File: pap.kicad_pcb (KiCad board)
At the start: 2 copper layers, 36 x 19 mm, 6 parts, among them J1 Conn_01x03

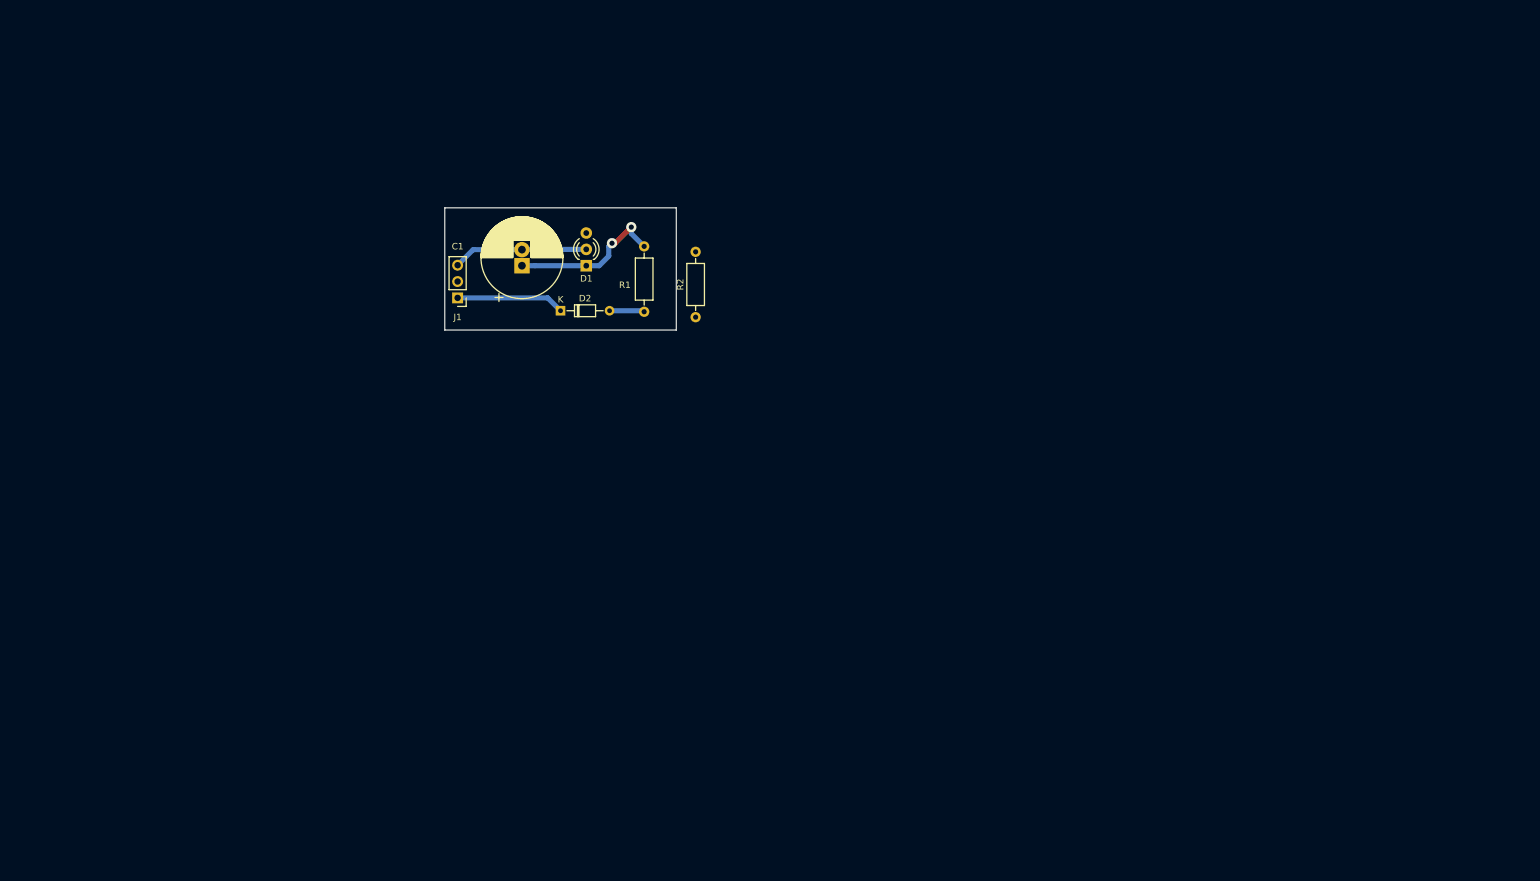
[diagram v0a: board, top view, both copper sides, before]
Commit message: agrego mas conectores y paso a pcb (todo mal!)
agregue conectores RJ45 para el encadenamiento spi y busyflag, pero no
para pulse.. es lo voy a mandar aparte porque es individual por cada
driver.. al igual que switch, y vere si alguna cosa mas.. en el rj me
sobran aun 2 pines.. ya vere que mando..lastima que no puedo mandar
pulse por ahi.. porque al ser 1 por driver necesito ir directo desde el
controlador.. sino como?... pase a pcb para ver que onda nada mas y
obvio me faltan definir los footprints de casi todo.. pero al menos
paso...orcad ya estaria llorando y no podria hacer nada...como sea, esta
bueno...sigo
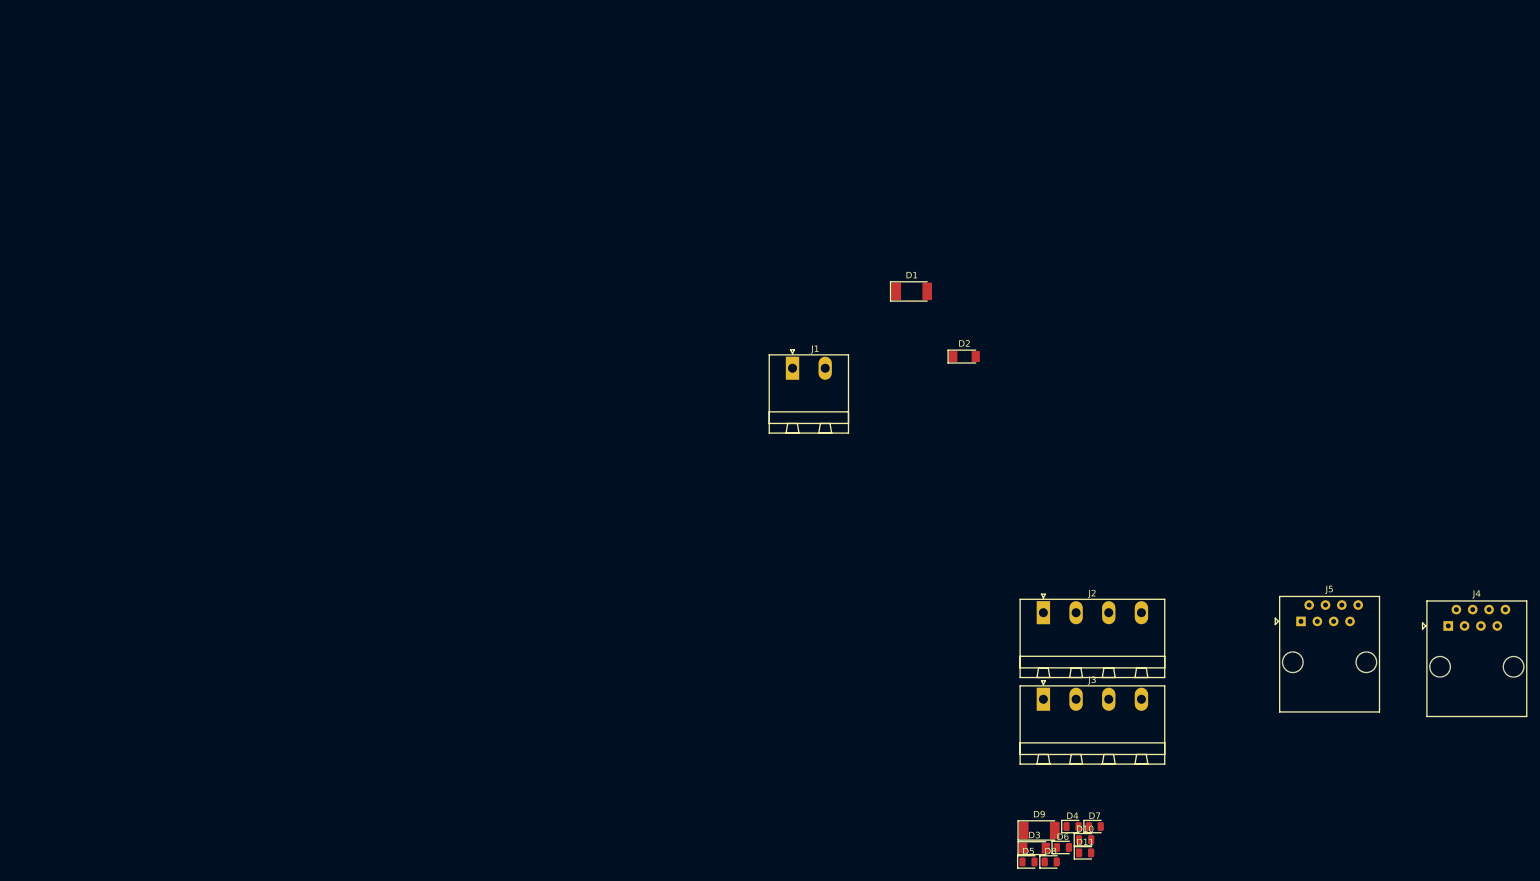
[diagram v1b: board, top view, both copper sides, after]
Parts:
- removed C1: 100n, Capacitor_THT:CP_Radial_D12.5mm_P2.50mm
- removed R1, R2: 100k, Resistor_THT:R_Axial_DIN0207_L6.3mm_D2.5mm_P10.16mm_Horizontal
- added D10: LED, LED_SMD:LED_0805_2012Metric, F.Cu at (221.5, 170.2)
- added D11: LED, LED_SMD:LED_0805_2012Metric, F.Cu at (221.5, 172.3)
- added D3: LL4148, Diode_SMD:D_MiniMELF, F.Cu at (213.7, 171.5)
- added D4: LED, LED_SMD:LED_0805_2012Metric, F.Cu at (219.6, 168.2)
- added D5: LED, LED_SMD:LED_0805_2012Metric, F.Cu at (212.7, 173.7)
- added D6: LED, LED_SMD:LED_0805_2012Metric, F.Cu at (218.1, 171.4)
- added D7: LED, LED_SMD:LED_0805_2012Metric, F.Cu at (223.0, 168.2)
- added D8: LED, LED_SMD:LED_0805_2012Metric, F.Cu at (216.2, 173.7)
- added D9: SM4007, Diode_SMD:D_MELF, F.Cu at (214.4, 168.8)
- added J2: Conn_01x04, Connector_Phoenix_MSTB:PhoenixContact_MSTBA_2,5_4-G-5,08_1x04_P5.08mm_Horizontal, F.Cu at (215.1, 134.9)
- added J3: Conn_01x04, Connector_Phoenix_MSTB:PhoenixContact_MSTBA_2,5_4-G-5,08_1x04_P5.08mm_Horizontal, F.Cu at (215.1, 148.4)
- added J4: RJ45, Connector_RJ:RJ45_Amphenol_54602-x08_Horizontal, F.Cu at (278.0, 137.0)
- added J5: RJ45, Connector_RJ:RJ45_Amphenol_54602-x08_Horizontal, F.Cu at (255.1, 136.3)
- D1: value led rojo 3mm -> SM4007; footprint LED_THT:LED_D3.0mm-3 -> Diode_SMD:D_MELF
- D2: value 1N4148 -> LL4148; footprint Diode_THT:D_DO-34_SOD68_P7.62mm_Horizontal -> Diode_SMD:D_MiniMELF
- J1: value Conn_01x03 -> Conn_01x02; footprint Connector_PinHeader_2.54mm:PinHeader_1x03_P2.54mm_Vertical -> Connector_Phoenix_MSTB:PhoenixContact_MSTBA_2,5_2-G-5,08_1x02_P5.08mm_Horizontal
- moved D2 63.2 mm to (202.8, 95.1)
- moved J1 53.2 mm to (176.1, 96.9), turned to 0 degrees
- moved D1 50.8 mm to (194.6, 85.0), turned to 0 degrees
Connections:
- D1 pad 1: Net-(C1-Pad1) -> +VDC
- D1 pad 2: Net-(C1-Pad2) -> GND
- D2 pad 1: Net-(D2-Pad1) -> Net-(C4-Pad1)
- J1 pad 1: Net-(D2-Pad1) -> GND
- J1 pad 2: Net-(J1-Pad2) -> +VDC
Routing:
- net Net-(C1-Pad1): track 24.2 -> 0.00 mm, vias 2 -> 0
- net Net-(C1-Pad2): track 21.0 -> 0.00 mm
- net Net-(D2-Pad1): track 16.8 -> 0.00 mm
- net Net-(C5-Pad2): track 5.45 -> 0.00 mm
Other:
- board outline removed

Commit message: armo huella step01 y asigno casi todas las huellas
ahi hice el landpattern del steo01, que es un parto, pero quedo bueno..
al tiempo que aprendi a editar y la verdad es que es comodo.. me animo a
decir que supera a allegro, y de hecho se parece demasiado en muchas
cosas.. huele a copia de algun lado.. incluiso los nombres en los menus
son iguales... como sea, ya quedo eso, lo que si tuve que volar algunos
pines repetidos en el simbolo porque sino era un chino tener muchos
pines repetidos, o sea en la huella tengo un pin que va a parar a
multiples pines en el esquemativo. si bien lo logre hacer superponiendo
encimados los pines en el esquemativo y dejandolos invisibles excepto
uno, eso funca, pero es un azco... preferi volar todos y dejar la union
univoca y listo.. al simbolo le faltan pines, pero el landpattern no los
necesita porque se unen todos en una misma masa de pad. despues pase
todas las huellas del resto del chiquitaje y ademas acomodo los power
netlist que estaban mal y de paso voy puliendo el disenio en general..
va quedando.. un poco mas y paso a tirar pista
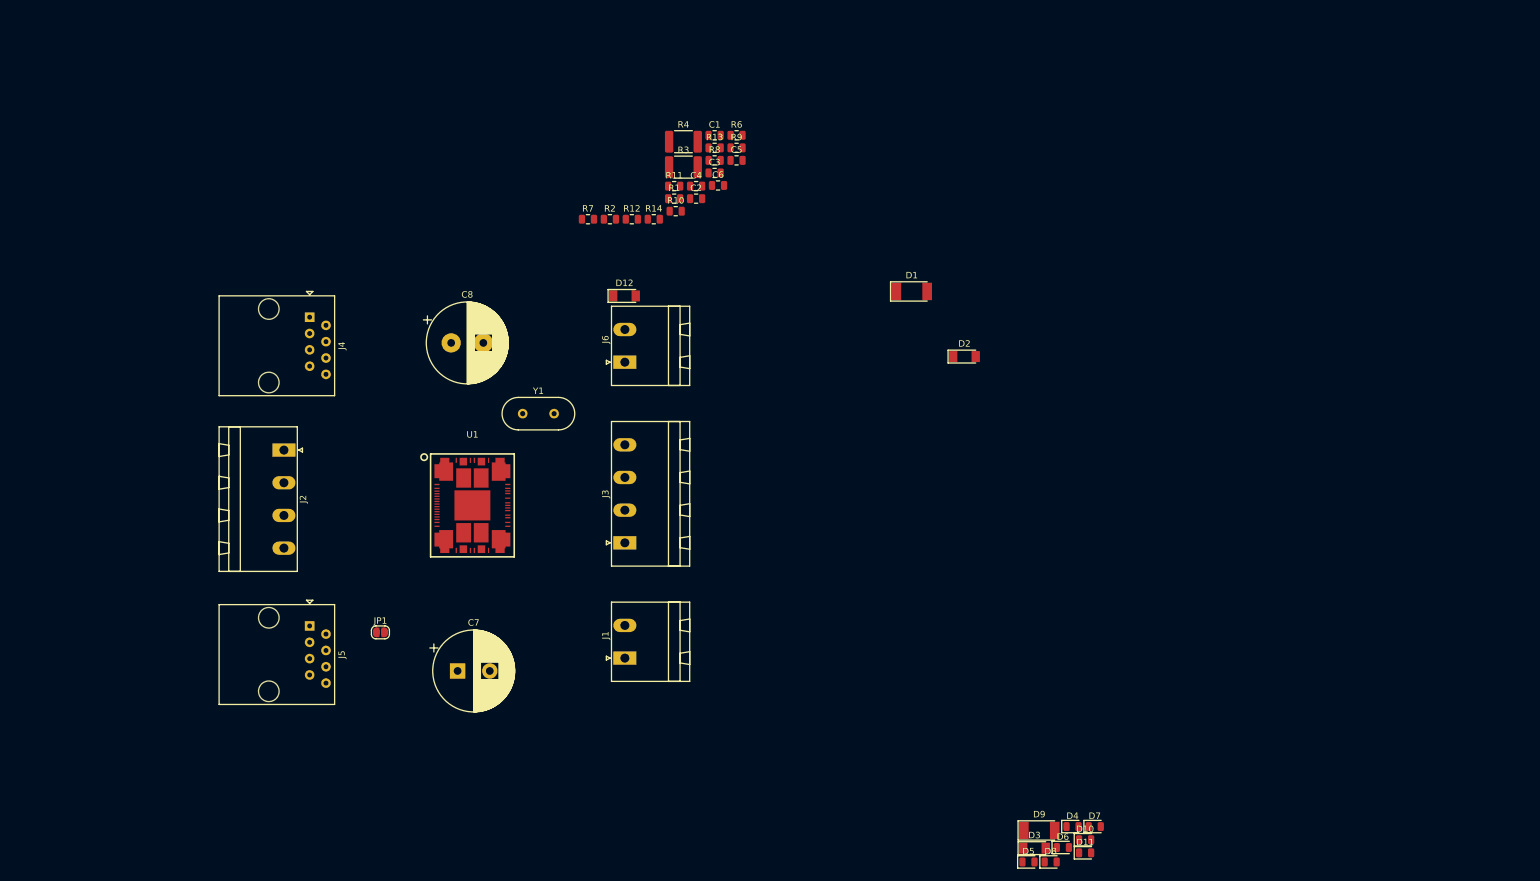
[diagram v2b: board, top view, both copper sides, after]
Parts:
- added C1: C, Capacitor_SMD:C_0805_2012Metric, F.Cu at (164.0, 60.7)
- added C2: 10pF, Capacitor_SMD:C_0805_2012Metric, F.Cu at (161.1, 70.6)
- added C3: 10pF, Capacitor_SMD:C_0805_2012Metric, F.Cu at (164.0, 66.6)
- added C4: C, Capacitor_SMD:C_0805_2012Metric, F.Cu at (161.1, 68.6)
- added C5: C, Capacitor_SMD:C_0805_2012Metric, F.Cu at (167.4, 64.6)
- added C6: C, Capacitor_SMD:C_0805_2012Metric, F.Cu at (164.5, 68.5)
- added C7: 100uFx100v, Capacitor_THT:CP_Radial_D12.5mm_P5.00mm, F.Cu at (124.0, 144.0)
- added C8: 100uFx100v, Capacitor_THT:CP_Radial_D12.5mm_P5.00mm, F.Cu at (123.0, 93.0)
- added D12: D_Zener, Diode_SMD:D_MiniMELF, F.Cu at (149.9, 85.7)
- added J6: Conn_01x02, Connector_Phoenix_MSTB:PhoenixContact_MSTBA_2,5_2-G-5,08_1x02_P5.08mm_Horizontal, F.Cu at (150.0, 96.0)
- added JP1: jumper, Jumper:SolderJumper-2_P1.3mm_Open_RoundedPad1.0x1.5mm, F.Cu at (112.0, 138.0)
- added R1: R, Resistor_SMD:R_0805_2012Metric, F.Cu at (157.7, 70.6)
- added R10: R, Resistor_SMD:R_0805_2012Metric, F.Cu at (157.9, 72.5)
- added R11: R, Resistor_SMD:R_0805_2012Metric, F.Cu at (157.7, 68.6)
- added R12: R, Resistor_SMD:R_0805_2012Metric, F.Cu at (151.1, 73.8)
- added R13: R, Resistor_SMD:R_0805_2012Metric, F.Cu at (164.0, 62.7)
- added R14: R, Resistor_SMD:R_0805_2012Metric, F.Cu at (154.5, 73.8)
- added R2: R, Resistor_SMD:R_0805_2012Metric, F.Cu at (147.7, 73.8)
- added R3: R, Resistor_SMD:R_1812_4532Metric_Pad1.30x3.40mm_HandSolder, F.Cu at (159.1, 65.7)
- added R4: R, Resistor_SMD:R_1812_4532Metric_Pad1.30x3.40mm_HandSolder, F.Cu at (159.1, 61.7)
- added R6: R, Resistor_SMD:R_0805_2012Metric, F.Cu at (167.4, 60.7)
- added R7: R, Resistor_SMD:R_0805_2012Metric, F.Cu at (144.3, 73.8)
- added R8: R, Resistor_SMD:R_0805_2012Metric, F.Cu at (164.0, 64.6)
- added R9: R, Resistor_SMD:R_0805_2012Metric, F.Cu at (167.4, 62.7)
- added U1: powerstep01, powerstep:powerstep, F.Cu at (126.3, 118.3)
- added Y1: 32Mhz, Crystal:Crystal_HC49-U_Vertical, F.Cu at (134.1, 104.0)
- moved J4 183.4 mm to (101.0, 89.0), turned to 270 degrees
- moved J5 154.1 mm to (101.0, 137.0), turned to 270 degrees
- moved J2 120.7 mm to (97.0, 109.7), turned to 270 degrees
- moved J3 69.5 mm to (150.0, 124.1), turned to 90 degrees
- moved J1 52.1 mm to (150.0, 142.0), turned to 90 degrees
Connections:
- D1 pad 1: +VDC -> 85v
- D1 pad 2: GND -> Net-(D1-Pad2)
- D3 pad 2: +VDC -> 85v
- D4 pad 2: +VDC -> 3v3
- D5 pad 2: +VDC -> 3v3
- D6 pad 2: +VDC -> 3v3
- D9 pad 1: +VDC -> 15v
- D9 pad 2: +VDC -> 3v3
- J1 pad 1: GND -> 85v
- J1 pad 2: +VDC -> 85v
- J2 pad 2: Net-(J2-Pad2) -> /connector/Busy
- J4 pad 7: /connector/Busy -> Net-(J4-Pad7)
- J4 pad 8: GND -> Net-(J4-Pad8)
- J5 pad 1: GND -> Net-(J5-Pad1)
- J5 pad 2: /connector/Busy -> Net-(J4-Pad7)

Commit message: arranco a rutear, cambio xtal por SMD y opcion CLKIN
arranque a tirar pist porque me estaba aburriendo ya, de paso voy
practivcando los shortcuts y demas.. esta muy copado y te aviso.. es
plagio a allegro.. no cabe dudas.. como sea, cambie el Xtal por uno SMD
de 4 pines que se consigue y minimiza el espacio, agegue tambien clkin
para mandar clk a todos por igual con el PWM del uC para sincronizar con
un selector para poder usar el xtal si es que el PWM se pierde por
fanout o ruido.. y no mucho mas
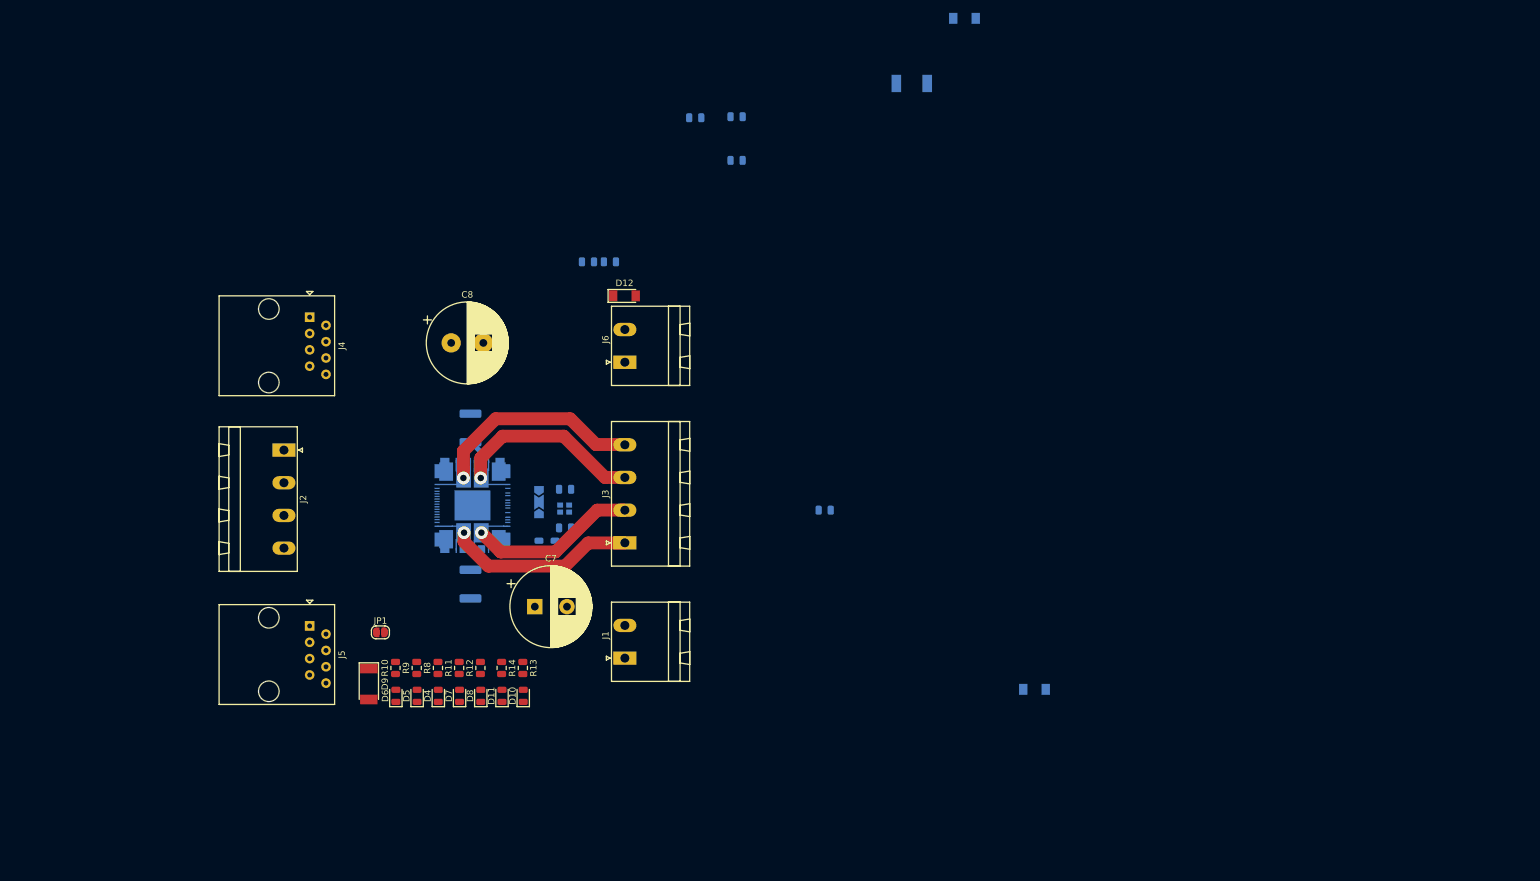
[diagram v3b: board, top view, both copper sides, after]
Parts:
- added JP2: Clk_Select, Jumper:SolderJumper-3_P2.0mm_Open_TrianglePad1.0x1.5mm, B.Cu at (136.6, 117.8)
- C1, C2, C3, C4, C5, C6, D1, D2, D3, R1, R2, R3, R4, R6, R7, U1: moved to B.Cu
- Y1: footprint Crystal:Crystal_HC49-U_Vertical -> Crystal:Crystal_SMD_2016-4Pin_2.0x1.6mm; moved to B.Cu
- moved D9 106.7 mm to (110.2, 146.0), turned to 270 degrees
- moved D6 106.3 mm to (114.4, 147.9), turned to 90 degrees
- moved D7 100.8 mm to (124.3, 147.9), turned to 90 degrees
- moved D4 100.7 mm to (121.0, 147.9), turned to 90 degrees
- moved D5 98.5 mm to (117.7, 147.9), turned to 90 degrees
- moved R9 94.9 mm to (117.6, 143.5), turned to 90 degrees
- moved D11 93.9 mm to (130.9, 147.9), turned to 90 degrees
- moved D8 92.3 mm to (127.6, 147.9), turned to 90 degrees
- moved D10 90.2 mm to (134.2, 147.9), turned to 90 degrees
- moved R8 89.9 mm to (120.9, 143.5), turned to 90 degrees
- moved R13 86.2 mm to (134.1, 143.5), turned to 270 degrees
- moved R10 83.3 mm to (114.3, 143.5), turned to 90 degrees
- moved R11 82.0 mm to (124.2, 143.5), turned to 90 degrees
- moved R14 73.7 mm to (130.8, 143.5), turned to 270 degrees
- moved R12 73.6 mm to (127.5, 143.5), turned to 90 degrees
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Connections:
- C1 pad 1: Net-(C1-Pad1) -> G3V3
- C2 pad 2: Net-(C2-Pad2) -> G3V3
- C3 pad 2: Net-(C3-Pad2) -> G3V3
- C6 pad 1: Net-(C6-Pad1) -> G85V
- C7 pad 2: Net-(C7-Pad2) -> G85V
- C8 pad 2: Net-(C8-Pad2) -> G85V
- D1 pad 2: Net-(D1-Pad2) -> G85V
- D12 pad 2: Net-(D12-Pad2) -> G85V
- J3 pad 1: /connector/MotorA1 -> /connector/MotorB2
- J3 pad 2: /connector/MotorA2 -> /connector/MotorB1
- J3 pad 3: /connector/MotorB2 -> /connector/MotorA1
- J3 pad 4: /connector/MotorB1 -> /connector/MotorA2
- J4 pad 5: Net-(J4-Pad5) -> /connector/CLKIN
- J4 pad 8: Net-(J4-Pad8) -> G3V3
- J5 pad 1: Net-(J5-Pad1) -> G3V3
- J5 pad 4: Net-(J5-Pad4) -> /connector/CLKIN
- J6 pad 1: Net-(J6-Pad1) -> G85V
- J6 pad 2: Net-(J6-Pad1) -> G85V
- R11 pad 1: Net-(R11-Pad1) -> G85V
- R12 pad 1: Net-(R12-Pad1) -> G85V
- R13 pad 1: Net-(R13-Pad1) -> G85V
- R14 pad 1: Net-(R14-Pad1) -> G85V
- R3 pad 2: Net-(R3-Pad2) -> G85V
- R4 pad 2: Net-(R4-Pad2) -> G85V
- R7 pad 2: Net-(R7-Pad2) -> G85V
- U1 pad 21: Net-(U1-Pad21) -> G3V3
- U1 pad 59: Net-(U1-Pad59) -> G85V
- U1 pad 63: Net-(C2-Pad1) -> Net-(JP2-Pad3)
- U1 pad 64: Net-(C3-Pad1) -> Net-(C2-Pad1)
- U1 pad 8: Net-(U1-Pad8) -> G3V3
- U1 pad 93: Net-(U1-Pad93) -> G85V
- Y1 pad 1: Net-(C3-Pad1) -> Net-(C2-Pad1)
- Y1 pad 2: Net-(C2-Pad1) -> G3V3
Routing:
- net /connector/MotorA2: track 0.00 -> 42.4 mm, vias 0 -> 1
- net /connector/MotorA1: track 0.00 -> 40.6 mm, vias 0 -> 1
- net /connector/MotorB2: track 0.00 -> 40.5 mm, vias 0 -> 1
- net /connector/MotorB1: track 0.00 -> 37.5 mm, vias 0 -> 1
- net Net-(R4-Pad1): track 0.00 -> 7.08 mm
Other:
- net class Default: clearance 0.8 -> 0.2; trace_width 0.8 -> 0.2; via_dia 1.6 -> 1; via_drill 0.8 -> 0.5
- rule pad_to_mask_clearance: 0.2 -> 0.125
- rule trace_clearance: 0.8 -> 0.2
- rule trace_min: 0.8 -> 0.2
- rule via_min_drill: 0.8 -> 0.5
- rule via_min_size: 1.6 -> 1
